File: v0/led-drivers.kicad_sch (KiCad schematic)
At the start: 37 parts, among them U5 TLC5971PWP, U6 TLC5971PWP, U7 LIS2DH

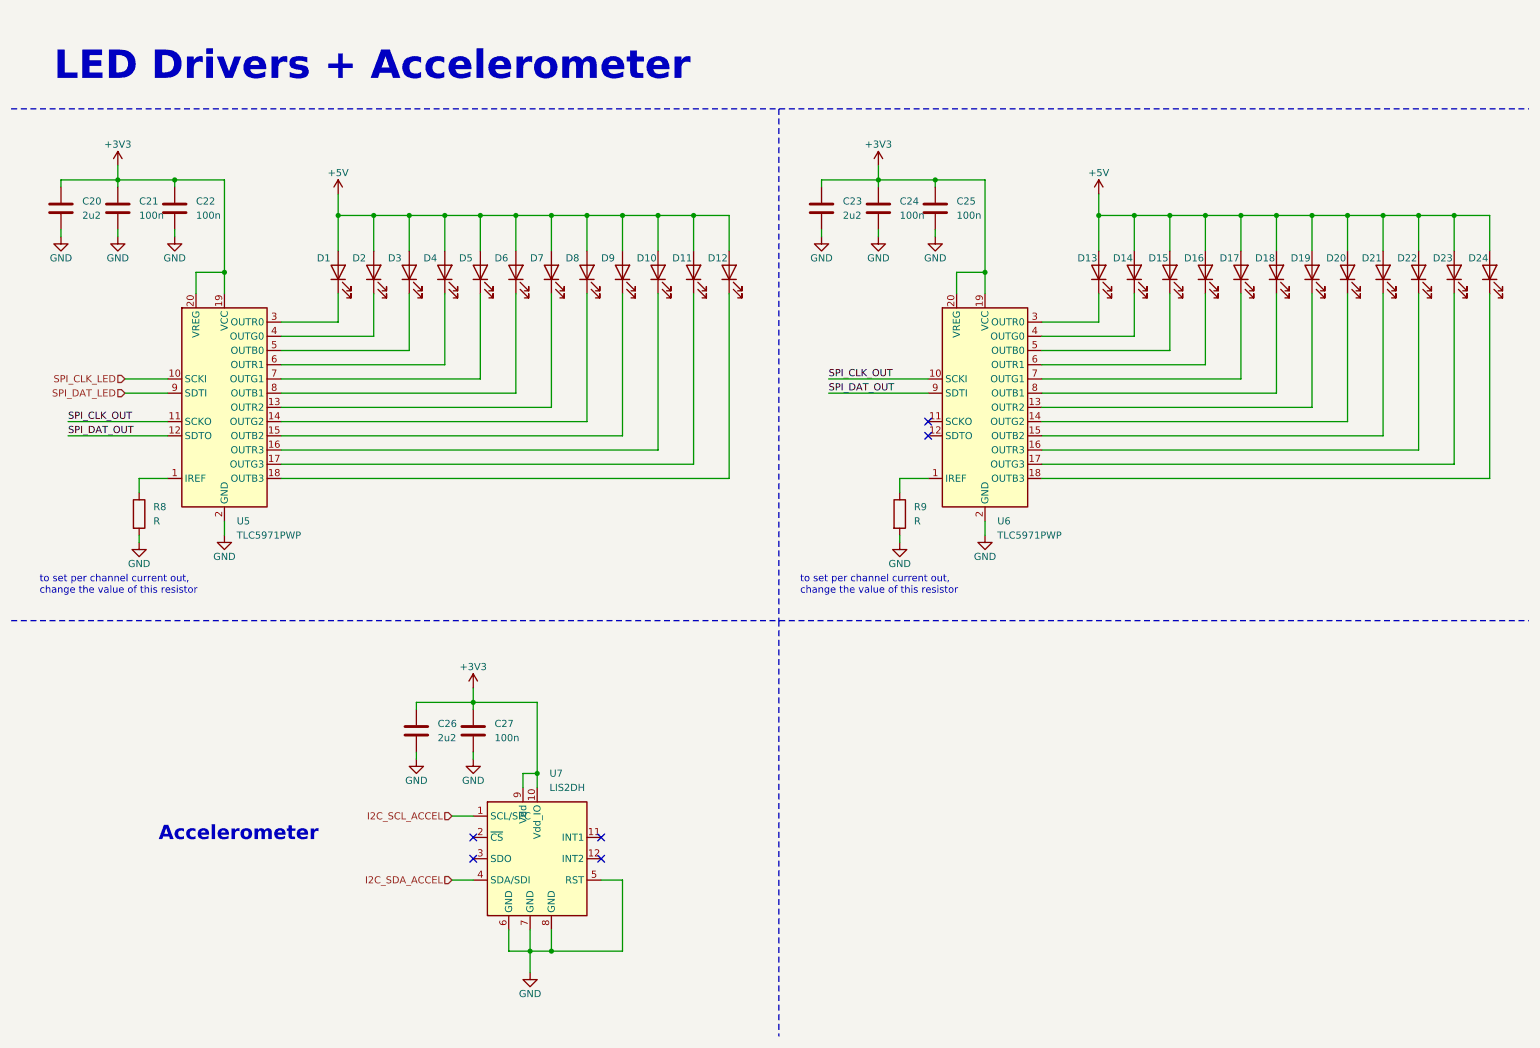
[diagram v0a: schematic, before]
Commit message: Picked new LED driver TLC59116, conected over I2C (instead of the previous one that used SPI), increased number of LEDs from 24 to 32.
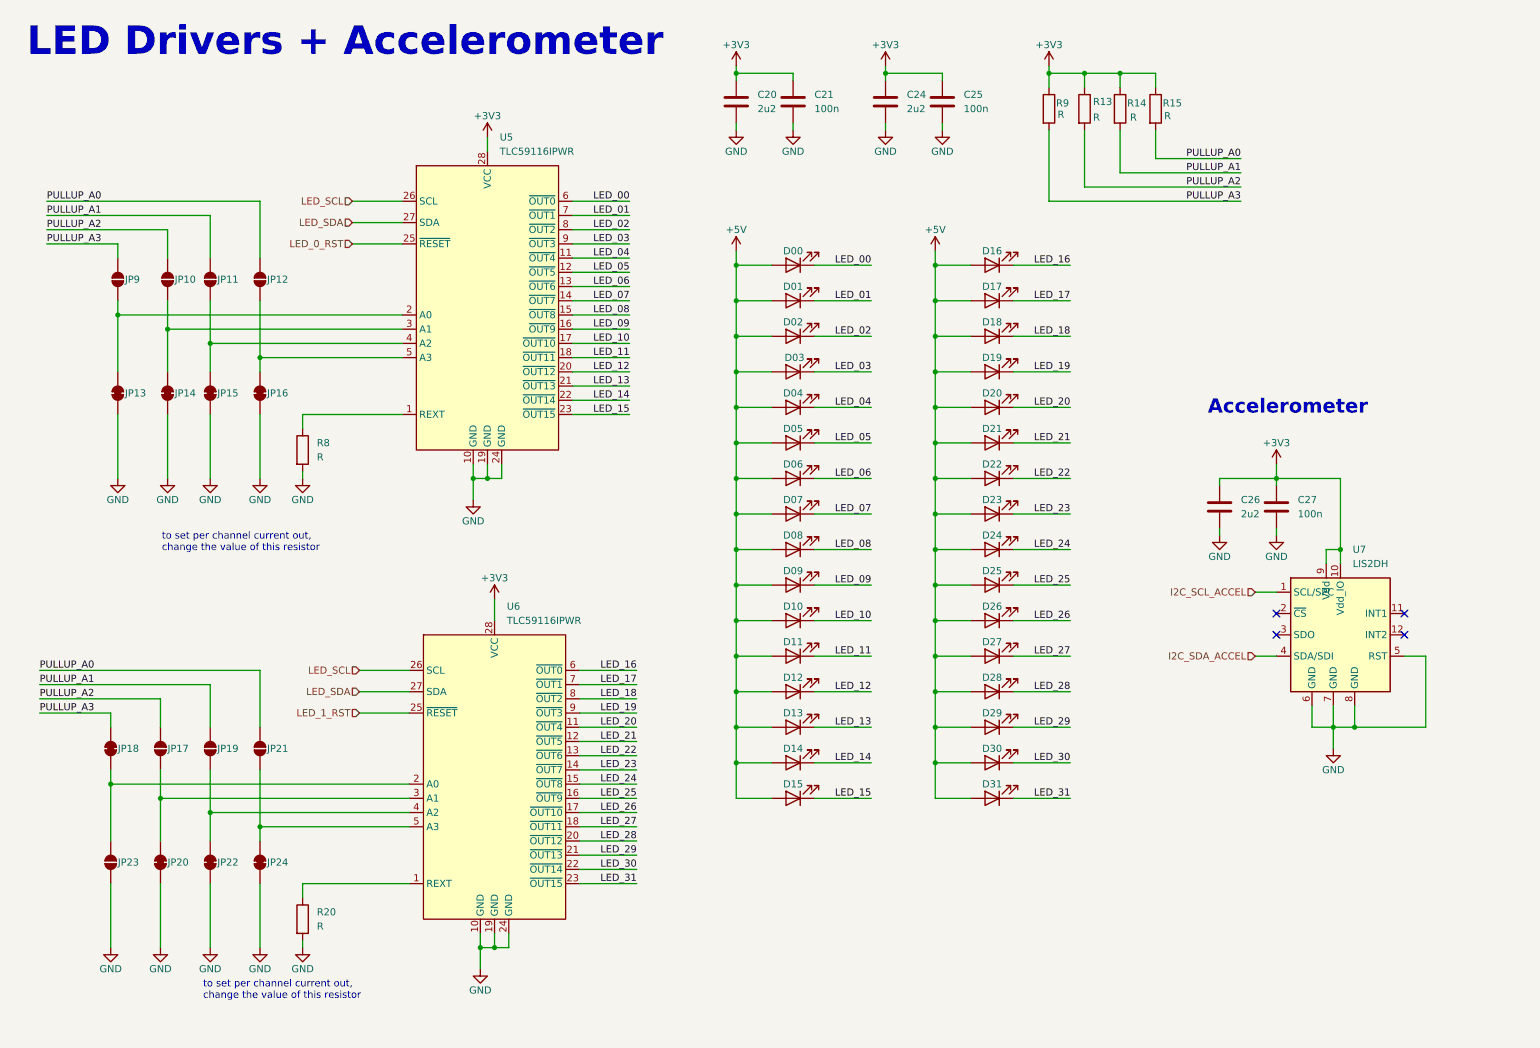
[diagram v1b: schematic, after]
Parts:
- removed C22, C24: 100n, Capacitor_SMD:C_0603_1608Metric, symbol jellybeans:C-0603-100n-50V
- removed C23: 2u2, Capacitor_SMD:C_0805_2012Metric, symbol jellybeans:C-0805-2u2-25V
- removed D1, D2, D3: LED, LED_SMD:LED_0805_2012Metric, symbol Device:LED
- removed D4, D5, D6, D7, D8, D9: LED, symbol Device:LED
- removed U5, U6: TLC5971PWP, Package_SO:HTSSOP-20-1EP_4.4x6.5mm_P0.65mm_EP3.4x6.5mm_Mask2.75x3.43mm_ThermalVias, symbol Driver_LED:TLC5971PWP
- added C24: 2u2, Capacitor_SMD:C_0805_2012Metric, symbol jellybeans:C-0805-2u2-25V
- added D00, D01, D02: LED, LED_SMD:LED_0805_2012Metric, symbol Device:LED
- added D03, D04, D05, D06, D07, D08, D09, D25, D26, D27, D28, D29, D30, D31: LED, symbol Device:LED
- added JP10, JP11, JP12, JP17, JP19, JP21, JP23, JP9: SolderJumper_2_Open, symbol Jumper:SolderJumper_2_Open
- added JP13, JP14, JP15, JP16, JP18, JP20, JP22, JP24: SolderJumper_2_Bridged, symbol Jumper:SolderJumper_2_Bridged
- added R13, R14, R15, R20: R, symbol Device:R
- added U5, U6: TLC59116IPWR, Package_SO:TSSOP-28_4.4x9.7mm_P0.65mm, symbol suchi_chips:TLC59116IPWR
- D16, D17, D18: footprint (none) -> LED_SMD:LED_0805_2012Metric
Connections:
- net +3V3: now also R9.1, C24.1, R13.1, R14.1, R15.1, U5.28 (VCC), U6.28 (VCC)
- net +5V: now also D00.2 (A), D01.2 (A), D02.2 (A), D03.2 (A), D04.2 (A), D05.2 (A), D06.2 (A), D07.2 (A), D08.2 (A), D09.2 (A), D25.2 (A), D26.2 (A), D27.2 (A), D28.2 (A), D29.2 (A), D30.2 (A), D31.2 (A)
- net GND: now also C24.2, JP13.1 (A), JP14.1 (A), JP15.1 (A), JP16.1 (A), JP20.1 (A), JP22.1 (A), JP23.1 (A), JP24.1 (A), R20.2, U5.10 (GND), U5.19 (GND), U5.24 (GND), U6.10 (GND), U6.19 (GND), U6.24 (GND); no longer R9.2
- net LED_15: now reaches D15.1 (K)
- net LED_15: now also U5.23 (~{OUT15})
- net LED_20: now reaches D20.1 (K)
- net LED_20: now also U6.11 (~{OUT4})
- net at R8.1: now also U5.1 (REXT)
- net LED_10: now reaches D10.1 (K)
- net LED_10: now also U5.17 (~{OUT10})
- net LED_11: now reaches D11.1 (K)
- net LED_11: now also U5.18 (~{OUT11})
- net LED_12: now reaches D12.1 (K)
- net LED_12: now also U5.20 (~{OUT12})
- net LED_21: now reaches D21.1 (K)
- net LED_21: now also U6.12 (~{OUT5})
- net LED_19: now reaches D19.1 (K)
- net LED_19: now also U6.9 (~{OUT3})
- net LED_22: now reaches D22.1 (K)
- net LED_22: now also U6.13 (~{OUT6})
- net LED_23: now reaches D23.1 (K)
- net LED_23: now also U6.14 (~{OUT7})
- net LED_24: now reaches D24.1 (K)
- net LED_24: now also U6.15 (~{OUT8})
- net LED_13: now reaches D13.1 (K)
- net LED_13: now also U5.21 (~{OUT13})
- net LED_14: now reaches D14.1 (K)
- net LED_14: now also U5.22 (~{OUT14})
- net LED_16: now reaches D16.1 (K)
- net LED_16: now also U6.6 (~{OUT0})
- net LED_17: now reaches D17.1 (K)
- net LED_17: now also U6.7 (~{OUT1})
- net LED_18: now reaches D18.1 (K)
- net LED_18: now also U6.8 (~{OUT2})
- new net: JP13.2 (B), JP9.1 (A), U5.2 (A0)
- new net: JP11.1 (A), JP15.2 (B), U5.4 (A2)
- new net: JP10.1 (A), JP14.2 (B), U5.3 (A1)
- new net: JP12.1 (A), JP16.2 (B), U5.5 (A3)
- new net: JP19.1 (A), JP22.2 (B), U6.4 (A2)
- new net: JP17.1 (A), JP20.2 (B), U6.3 (A1)
- new net: R20.1, U6.1 (REXT)
- new net: JP18.1 (A), JP23.2 (B), U6.2 (A0)
- new net: JP21.1 (A), JP24.2 (B), U6.5 (A3)
- new net LED_00: D00.1 (K), U5.6 (~{OUT0})
- new net LED_01: D01.1 (K), U5.7 (~{OUT1})
- new net LED_02: D02.1 (K), U5.8 (~{OUT2})
- new net LED_03: D03.1 (K), U5.9 (~{OUT3})
- new net LED_04: D04.1 (K), U5.11 (~{OUT4})
- new net LED_05: D05.1 (K), U5.12 (~{OUT5})
- new net LED_06: D06.1 (K), U5.13 (~{OUT6})
- new net LED_07: D07.1 (K), U5.14 (~{OUT7})
- new net LED_08: D08.1 (K), U5.15 (~{OUT8})
- new net LED_09: D09.1 (K), U5.16 (~{OUT9})
- new net LED_0_RST: U5.25 (~{RESET})
- new net LED_1_RST: U6.25 (~{RESET})
- new net LED_25: D25.1 (K), U6.16 (~{OUT9})
- new net LED_26: D26.1 (K), U6.17 (~{OUT10})
- new net LED_27: D27.1 (K), U6.18 (~{OUT11})
- new net LED_28: D28.1 (K), U6.20 (~{OUT12})
- new net LED_29: D29.1 (K), U6.21 (~{OUT13})
- new net LED_30: D30.1 (K), U6.22 (~{OUT14})
- new net LED_31: D31.1 (K), U6.23 (~{OUT15})
- new net LED_SCL: U5.26 (SCL), U6.26 (SCL)
- new net LED_SDA: U5.27 (SDA), U6.27 (SDA)
- new net PULLUP_A0: JP12.2 (B), JP21.2 (B), R15.2
- new net PULLUP_A1: JP11.2 (B), JP19.2 (B), R14.2
- new net PULLUP_A2: JP10.2 (B), JP17.2 (B), R13.2
- new net PULLUP_A3: JP18.2 (B), JP9.2 (B), R9.2
- no-connect marks 6 -> 4
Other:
- moved on the sheet: C26, C27, R8, U7
